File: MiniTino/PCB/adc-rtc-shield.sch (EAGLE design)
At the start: 57 parts, among them IC1 TLC2543, IC2 RV_3049_C2

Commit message: Aktualisiert.
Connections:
- net +5V: now also U$1.VCC
- net A6: now also U$1.A6
- net A7: now also U$1.A7
- net AD0: now also U$1.A0
- net AD1: now also U$1.A1
- net AD2: now also U$1.A2
- net AD3: now also U$1.A3
- net AD4/SDA: now also U$1.A4
- net AD5/SCL: now also U$1.A5
- net GND: now also U$1.GND@2
- net IO0: now also U$1.RXI
- net IO1: now also U$1.TXO
- net IO2: now also U$1.2
- net IO3: now also U$1.*3
- net IO4: now also U$1.4
- net IO5: now also U$1.*5
- net IO6: now also U$1.*6
- net IO7: now also U$1.7
- net IO8: now also U$1.8
- net IO9: now also U$1.*9
- net MISO: now also U$1.12
- net MOSI: now also U$1.*11
- net RESET: now also U$1.RST
- net SCK: now also U$1.13
- net SS: now also U$1.*10
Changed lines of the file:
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@@
 <wire x1="320.04" y1="185.42" x2="320.04" y2="177.8" width="0.1524" layer="91"/>
 <junction x="320.04" y="177.8"/>
+<pinref part="U$1" gate="G$1" pin="VCC"/>
 </segment>
 <segment>
@@
 <wire x1="289.56" y1="210.82" x2="264.16" y2="210.82" width="0.1524" layer="91"/>
 <label x="281.94" y="210.82" size="1.778" layer="95"/>
+<pinref part="U$1" gate="G$1" pin="GND@2"/>
 </segment>
 <segment>
@@
 <wire x1="264.16" y1="193.04" x2="289.56" y2="193.04" width="0.1524" layer="91"/>
 <label x="281.94" y="193.04" size="1.778" layer="95"/>
+<pinref part="U$1" gate="G$1" pin="13"/>
 </segment>
 <segment>
@@
 <wire x1="264.16" y1="190.5" x2="289.56" y2="190.5" width="0.1524" layer="91"/>
 <label x="281.94" y="190.5" size="1.778" layer="95"/>
+<pinref part="U$1" gate="G$1" pin="12"/>
 </segment>
 <segment>
@@
 <wire x1="289.56" y1="187.96" x2="264.16" y2="187.96" width="0.1524" layer="91"/>
 <label x="281.94" y="187.96" size="1.778" layer="95"/>
+<pinref part="U$1" gate="G$1" pin="*11"/>
 </segment>
 <segment>
@@
 <wire x1="264.16" y1="185.42" x2="289.56" y2="185.42" width="0.1524" layer="91"/>
 <label x="281.94" y="185.42" size="1.778" layer="95"/>
+<pinref part="U$1" gate="G$1" pin="*10"/>
 </segment>
 </net>
@@
 <wire x1="289.56" y1="195.58" x2="264.16" y2="195.58" width="0.1524" layer="91"/>
 <label x="281.94" y="195.58" size="1.778" layer="95"/>
+<pinref part="U$1" gate="G$1" pin="A0"/>
 </segment>
 </net>
@@
 <wire x1="264.16" y1="198.12" x2="289.56" y2="198.12" width="0.1524" layer="91"/>
 <label x="281.94" y="198.12" size="1.778" layer="95"/>
+<pinref part="U$1" gate="G$1" pin="A1"/>
 </segment>
 </net>
@@
 <wire x1="289.56" y1="200.66" x2="264.16" y2="200.66" width="0.1524" layer="91"/>
 <label x="281.94" y="200.66" size="1.778" layer="95"/>
+<pinref part="U$1" gate="G$1" pin="A2"/>
 </segment>
 </net>
@@
 <wire x1="264.16" y1="203.2" x2="289.56" y2="203.2" width="0.1524" layer="91"/>
 <label x="281.94" y="203.2" size="1.778" layer="95"/>
+<pinref part="U$1" gate="G$1" pin="A3"/>
 </segment>
 </net>
@@
 <wire x1="241.3" y1="180.34" x2="215.9" y2="180.34" width="0.1524" layer="91"/>
 <label x="218.44" y="180.34" size="1.778" layer="95"/>
+<pinref part="U$1" gate="G$1" pin="A4"/>
 </segment>
 <segment>
@@
 <wire x1="241.3" y1="177.8" x2="215.9" y2="177.8" width="0.1524" layer="91"/>
 <label x="218.44" y="177.8" size="1.778" layer="95"/>
+<pinref part="U$1" gate="G$1" pin="A5"/>
 </segment>
 <segment>
@@
 <wire x1="241.3" y1="203.2" x2="215.9" y2="203.2" width="0.1524" layer="91"/>
 <label x="218.44" y="203.2" size="1.778" layer="95"/>
+<pinref part="U$1" gate="G$1" pin="2"/>
 </segment>
 </net>
@@
 <wire x1="215.9" y1="213.36" x2="241.3" y2="213.36" width="0.1524" layer="91"/>
 <label x="218.44" y="213.36" size="1.778" layer="95"/>
+<pinref part="U$1" gate="G$1" pin="TXO"/>
 </segment>
 </net>
@@
 <wire x1="241.3" y1="210.82" x2="215.9" y2="210.82" width="0.1524" layer="91"/>
 <label x="218.44" y="210.82" size="1.778" layer="95"/>
+<pinref part="U$1" gate="G$1" pin="RXI"/>
 </segment>
 </net>
@@
 <wire x1="215.9" y1="200.66" x2="241.3" y2="200.66" width="0.1524" layer="91"/>
 <label x="218.44" y="200.66" size="1.778" layer="95"/>
+<pinref part="U$1" gate="G$1" pin="*3"/>
 </segment>
 </net>
@@
 <wire x1="241.3" y1="198.12" x2="215.9" y2="198.12" width="0.1524" layer="91"/>
 <label x="218.44" y="198.12" size="1.778" layer="95"/>
+<pinref part="U$1" gate="G$1" pin="4"/>
 </segment>
 </net>
@@
 <wire x1="215.9" y1="195.58" x2="241.3" y2="195.58" width="0.1524" layer="91"/>
 <label x="218.44" y="195.58" size="1.778" layer="95"/>
+<pinref part="U$1" gate="G$1" pin="*5"/>
 </segment>
 </net>
@@
 <wire x1="241.3" y1="193.04" x2="215.9" y2="193.04" width="0.1524" layer="91"/>
 <label x="218.44" y="193.04" size="1.778" layer="95"/>
+<pinref part="U$1" gate="G$1" pin="*6"/>
 </segment>
 </net>
@@
 <wire x1="215.9" y1="190.5" x2="241.3" y2="190.5" width="0.1524" layer="91"/>
 <label x="218.44" y="190.5" size="1.778" layer="95"/>
+<pinref part="U$1" gate="G$1" pin="7"/>
 </segment>
 </net>
@@
 <wire x1="215.9" y1="187.96" x2="241.3" y2="187.96" width="0.1524" layer="91"/>
 <label x="218.44" y="187.96" size="1.778" layer="95"/>
+<pinref part="U$1" gate="G$1" pin="8"/>
 </segment>
 </net>
@@
 <wire x1="241.3" y1="185.42" x2="215.9" y2="185.42" width="0.1524" layer="91"/>
 <label x="218.44" y="185.42" size="1.778" layer="95"/>
+<pinref part="U$1" gate="G$1" pin="*9"/>
 </segment>
 </net>
@@
 <wire x1="241.3" y1="208.28" x2="215.9" y2="208.28" width="0.1524" layer="91"/>
 <label x="218.44" y="208.28" size="1.778" layer="95"/>
+<pinref part="U$1" gate="G$1" pin="RST"/>
 </segment>
 </net>
@@
 <wire x1="289.56" y1="177.8" x2="264.16" y2="177.8" width="0.1524" layer="91"/>
 <label x="281.94" y="177.8" size="1.778" layer="95"/>
+<pinref part="U$1" gate="G$1" pin="A6"/>
 </segment>
 </net>
@@
 <wire x1="289.56" y1="180.34" x2="264.16" y2="180.34" width="0.1524" layer="91"/>
 <label x="281.94" y="180.34" size="1.778" layer="95"/>
-</segment>
-</net>
+<pinref part="U$1" gate="G$1" pin="A7"/>
+</segment>
+</net>

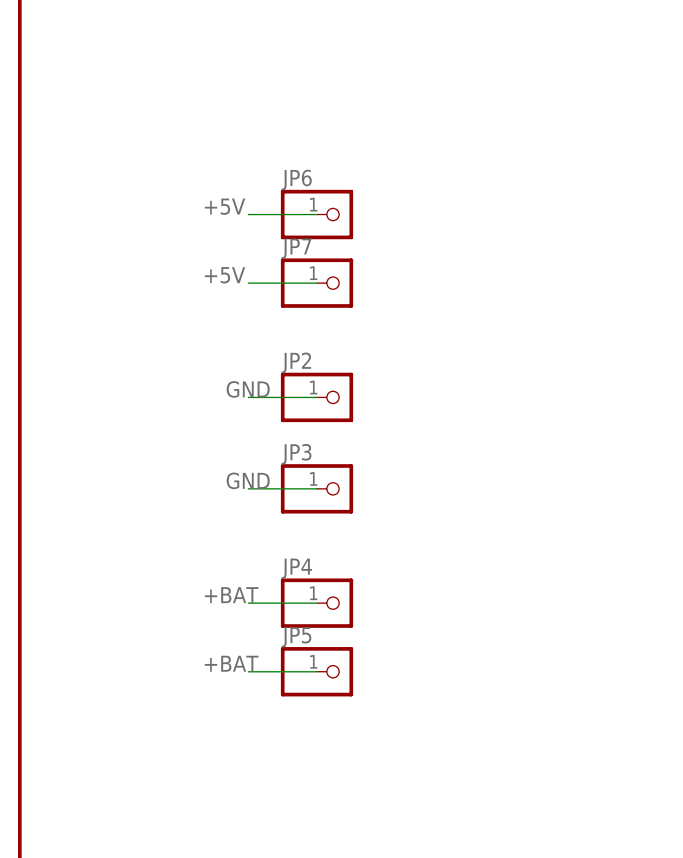
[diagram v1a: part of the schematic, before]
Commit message: Change resistor packages.
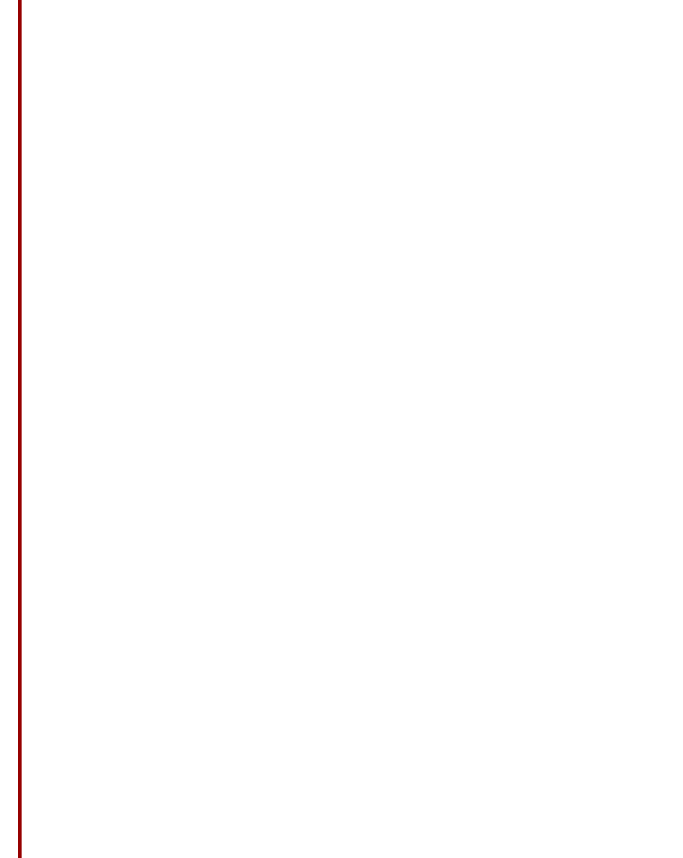
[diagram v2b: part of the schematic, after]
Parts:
- removed JP2, JP3, JP4, JP5, JP6, JP7: (no value), pinhead:PINHD-1X1
- R10, R13, R14, R15, R16, R17, R4, R5, R6, R8, R9: device resistor:R-EU_0207/10 -> resistor:R-EU_R0603
- R11, R12, R18, R19, R2, R20, R21, R3, R7: device resistor:R-EU_0207/12 -> resistor:R-EU_R0603
- R22: device rcl:R-EU_0207/10 -> rcl:R-EU_R0603
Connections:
- net +5V: no longer JP6.1, JP7.1
- net +BAT: no longer JP4.1, JP5.1
- net GND: no longer JP2.1, JP3.1

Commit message: Start routing.
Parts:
- removed JP8: (no value), pinhead:PINHD-1X2
- added JP2: (no value), pinhead:PINHD-1X8/90
- JP1: value 9x1F-H8.5 -> (none); device pinhead:PINHD-1X9/90 -> pinhead:PINHD-2X8/90
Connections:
- net +3V3: now also JP2.2
- net +5V: now also JP2.1
- net A6: now also JP2.7; no longer JP8.1
- net A7: now also JP2.8; no longer JP8.2
- net GND: now also JP1.10, JP1.12, JP1.14, JP1.16, JP1.2, JP1.4, JP1.6, JP1.8, JP2.3; no longer JP1.1
- net IO0: now also JP2.5
- net IO1: now also JP2.4
- net RESET: now also JP2.6
- net X1_RX4-: now also JP1.15; no longer JP1.9
- net X2_TX4-: now also JP1.13; no longer JP1.8
- net X3_RX3-: now also JP1.11; no longer JP1.7
- net X4_TX3-: now also JP1.9; no longer JP1.6
- net X5_RX2-: now also JP1.7; no longer JP1.5
- net X6_TX2-: now also JP1.5; no longer JP1.4
- net X8_TX1-: now also JP1.1; no longer JP1.2
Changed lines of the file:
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@@
 <part name="P+3" library="supply1" deviceset="+5V" device=""/>
 <part name="P+5" library="supply1" deviceset="+5V" device=""/>
-<part name="JP1" library="pinhead" deviceset="PINHD-1X9" device="/90" value="9x1F-H8.5"/>
 <part name="U$1" library="SparkFun-Boards" deviceset="ARDUINO_PRO_MINI" device=""/>
-<part name="JP8" library="pinhead" deviceset="PINHD-1X2" device=""/>
+<part name="JP1" library="pinhead" deviceset="PINHD-2X8" device="/90"/>
+<part name="JP2" library="pinhead" deviceset="PINHD-1X8" device="/90"/>
 </parts>
 <sheets>
@@
 <instance part="R21" gate="G$1" x="116.84" y="88.9"/>
 <instance part="U$5" gate="G$1" x="203.2" y="55.88"/>
-<instance part="U$7" gate="G$1" x="71.12" y="78.74"/>
+<instance part="U$7" gate="G$1" x="40.64" y="78.74"/>
 <instance part="IC2" gate="A" x="129.54" y="203.2"/>
 <instance part="R22" gate="G$1" x="165.1" y="208.28" smashed="yes" rot="MR90">
@@
 <attribute name="VALUE" x="212.725" y="121.92" size="1.778" layer="96" rot="R180"/>
 </instance>
+<instance part="U$1" gate="G$1" x="251.46" y="198.12"/>
 <instance part="JP1" gate="A" x="55.88" y="96.52" rot="R180"/>
-<instance part="U$1" gate="G$1" x="251.46" y="198.12"/>
-<instance part="JP8" gate="G$1" x="330.2" y="205.74"/>
+<instance part="JP2" gate="A" x="330.2" y="231.14"/>
 </instances>
 <busses>
@@
 <junction x="320.04" y="177.8"/>
 <pinref part="U$1" gate="G$1" pin="VCC"/>
+<wire x1="327.66" y1="241.3" x2="307.34" y2="241.3" width="0.1524" layer="91"/>
+<label x="307.34" y="241.3" size="1.778" layer="95"/>
+<pinref part="JP2" gate="A" pin="1"/>
 </segment>
 <segment>
@@
 <pinref part="POWER" gate="A" pin="6"/>
 <pinref part="POWER" gate="A" pin="7"/>
+<wire x1="327.66" y1="236.22" x2="307.34" y2="236.22" width="0.1524" layer="91"/>
+<label x="307.34" y="236.22" size="1.778" layer="95"/>
+<pinref part="JP2" gate="A" pin="3"/>
 </segment>
 <segment>
@@
 <segment>
 <pinref part="U$7" gate="G$1" pin="GND"/>
-<wire x1="58.42" y1="86.36" x2="71.12" y2="86.36" width="0.1524" layer="91"/>
-<wire x1="71.12" y1="86.36" x2="71.12" y2="81.28" width="0.1524" layer="91"/>
-<pinref part="JP1" gate="A" pin="1"/>
+<wire x1="50.8" y1="106.68" x2="40.64" y2="106.68" width="0.1524" layer="91"/>
+<wire x1="40.64" y1="106.68" x2="40.64" y2="104.14" width="0.1524" layer="91"/>
+<wire x1="40.64" y1="104.14" x2="40.64" y2="101.6" width="0.1524" layer="91"/>
+<wire x1="40.64" y1="101.6" x2="40.64" y2="99.06" width="0.1524" layer="91"/>
+<wire x1="40.64" y1="99.06" x2="40.64" y2="96.52" width="0.1524" layer="91"/>
+<wire x1="40.64" y1="96.52" x2="40.64" y2="93.98" width="0.1524" layer="91"/>
+<wire x1="40.64" y1="93.98" x2="40.64" y2="91.44" width="0.1524" layer="91"/>
+<wire x1="40.64" y1="91.44" x2="40.64" y2="88.9" width="0.1524" layer="91"/>
+<wire x1="40.64" y1="88.9" x2="40.64" y2="81.28" width="0.1524" layer="91"/>
+<wire x1="50.8" y1="91.44" x2="40.64" y2="91.44" width="0.1524" layer="91"/>
+<wire x1="50.8" y1="93.98" x2="40.64" y2="93.98" width="0.1524" layer="91"/>
+<wire x1="50.8" y1="96.52" x2="40.64" y2="96.52" width="0.1524" layer="91"/>
+<wire x1="50.8" y1="99.06" x2="40.64" y2="99.06" width="0.1524" layer="91"/>
+<wire x1="50.8" y1="101.6" x2="40.64" y2="101.6" width="0.1524" layer="91"/>
+<wire x1="50.8" y1="104.14" x2="40.64" y2="104.14" width="0.1524" layer="91"/>
+<junction x="40.64" y="104.14"/>
+<junction x="40.64" y="101.6"/>
+<junction x="40.64" y="99.06"/>
+<junction x="40.64" y="96.52"/>
+<junction x="40.64" y="93.98"/>
+<junction x="40.64" y="91.44"/>
+<wire x1="50.8" y1="88.9" x2="40.64" y2="88.9" width="0.1524" layer="91"/>
+<junction x="40.64" y="88.9"/>
+<pinref part="JP1" gate="A" pin="2"/>
+<pinref part="JP1" gate="A" pin="4"/>
+<pinref part="JP1" gate="A" pin="6"/>
+<pinref part="JP1" gate="A" pin="8"/>
+<pinref part="JP1" gate="A" pin="10"/>
+<pinref part="JP1" gate="A" pin="12"/>
+<pinref part="JP1" gate="A" pin="14"/>
+<pinref part="JP1" gate="A" pin="16"/>
 </segment>
 </net>
@@
 <label x="307.34" y="180.34" size="1.778" layer="95"/>
 <pinref part="POWER" gate="A" pin="4"/>
+<wire x1="327.66" y1="238.76" x2="307.34" y2="238.76" width="0.1524" layer="91"/>
+<label x="307.34" y="238.76" size="1.778" layer="95"/>
+<pinref part="JP2" gate="A" pin="2"/>
 </segment>
 </net>
@@
 <label x="218.44" y="213.36" size="1.778" layer="95"/>
 <pinref part="U$1" gate="G$1" pin="TXO"/>
+<wire x1="307.34" y1="233.68" x2="327.66" y2="233.68" width="0.1524" layer="91"/>
+<label x="307.34" y="233.68" size="1.778" layer="95"/>
+<pinref part="JP2" gate="A" pin="4"/>
 </segment>
 </net>
@@
 <label x="218.44" y="210.82" size="1.778" layer="95"/>
 <pinref part="U$1" gate="G$1" pin="RXI"/>
+<wire x1="327.66" y1="231.14" x2="307.34" y2="231.14" width="0.1524" layer="91"/>
+<label x="307.34" y="231.14" size="1.778" layer="95"/>
+<pinref part="JP2" gate="A" pin="5"/>
 </segment>
 </net>
@@
 <pinref part="C12" gate="G$1" pin="2"/>
 <wire x1="58.42" y1="104.14" x2="104.14" y2="104.14" width="0.1524" layer="91"/>
-<pinref part="JP1" gate="A" pin="8"/>
+<pinref part="JP1" gate="A" pin="13"/>
 </segment>
 </net>
@@
 <pinref part="C13" gate="G$1" pin="2"/>
 <wire x1="58.42" y1="106.68" x2="107.95" y2="106.68" width="0.1524" layer="91"/>
-<pinref part="JP1" gate="A" pin="9"/>
+<pinref part="JP1" gate="A" pin="15"/>
 </segment>
 </net>
@@
 <pinref part="C11" gate="G$1" pin="2"/>
 <wire x1="58.42" y1="99.06" x2="96.52" y2="99.06" width="0.1524" layer="91"/>
-<pinref part="JP1" gate="A" pin="6"/>
+<pinref part="JP1" gate="A" pin="9"/>
 </segment>
 </net>
@@
 <pinref part="C10" gate="G$1" pin="2"/>
 <wire x1="58.42" y1="101.6" x2="100.33" y2="101.6" width="0.1524" layer="91"/>
-<pinref part="JP1" gate="A" pin="7"/>
+<pinref part="JP1" gate="A" pin="11"/>
 </segment>
 </net>
@@
 <pinref part="C22" gate="G$1" pin="2"/>
 <pinref part="R21" gate="G$1" pin="1"/>
-<pinref part="JP1" gate="A" pin="2"/>
+<pinref part="JP1" gate="A" pin="1"/>
 </segment>
 </net>
@@
 <pinref part="R15" gate="G$1" pin="1"/>
 <pinref part="R19" gate="G$1" pin="1"/>
-<pinref part="JP1" gate="A" pin="4"/>
+<pinref part="JP1" gate="A" pin="5"/>
 </segment>
 </net>
@@
 <pinref part="C19" gate="G$1" pin="2"/>
 <pinref part="R18" gate="G$1" pin="1"/>
-<pinref part="JP1" gate="A" pin="5"/>
+<pinref part="JP1" gate="A" pin="7"/>
 </segment>
 </net>
@@
 <label x="218.44" y="208.28" size="1.778" layer="95"/>
 <pinref part="U$1" gate="G$1" pin="RST"/>
+<wire x1="327.66" y1="228.6" x2="307.34" y2="228.6" width="0.1524" layer="91"/>
+<label x="307.34" y="228.6" size="1.778" layer="95"/>
+<pinref part="JP2" gate="A" pin="6"/>
 </segment>
 </net>
 <net name="A6" class="0">
 <segment>
-<pinref part="JP8" gate="G$1" pin="1"/>
-<wire x1="327.66" y1="208.28" x2="307.34" y2="208.28" width="0.1524" layer="91"/>
-<label x="309.88" y="208.28" size="1.778" layer="95"/>
+<wire x1="327.66" y1="226.06" x2="307.34" y2="226.06" width="0.1524" layer="91"/>
+<label x="307.34" y="226.06" size="1.778" layer="95"/>
 <wire x1="289.56" y1="177.8" x2="264.16" y2="177.8" width="0.1524" layer="91"/>
 <label x="281.94" y="177.8" size="1.778" layer="95"/>
 <pinref part="U$1" gate="G$1" pin="A6"/>
+<pinref part="JP2" gate="A" pin="7"/>
 </segment>
 </net>
 <net name="A7" class="0">
 <segment>
-<pinref part="JP8" gate="G$1" pin="2"/>
-<wire x1="327.66" y1="205.74" x2="307.34" y2="205.74" width="0.1524" layer="91"/>
-<label x="309.88" y="205.74" size="1.778" layer="95"/>
+<wire x1="327.66" y1="223.52" x2="307.34" y2="223.52" width="0.1524" layer="91"/>
+<label x="307.34" y="223.52" size="1.778" layer="95"/>
 <wire x1="289.56" y1="180.34" x2="264.16" y2="180.34" width="0.1524" layer="91"/>
 <label x="281.94" y="180.34" size="1.778" layer="95"/>
 <pinref part="U$1" gate="G$1" pin="A7"/>
-</segment>
-</net>
+<pinref part="JP2" gate="A" pin="8"/>
+</segment>
+</net>
